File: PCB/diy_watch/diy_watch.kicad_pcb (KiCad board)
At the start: 4 copper layers, 35.9 x 36.9 mm, 48 parts, among them IC1 W25Q16JVUXIQ, J1 USB_B_Micro, SW1 SW_Push, U1 FTE-2CA-V-T/R, U2 DS3231MZ, U3 RP2040, U7 XC6210B332MR, U8 LTC4071EMS8E_PBF, Y1 12MHz_crystal

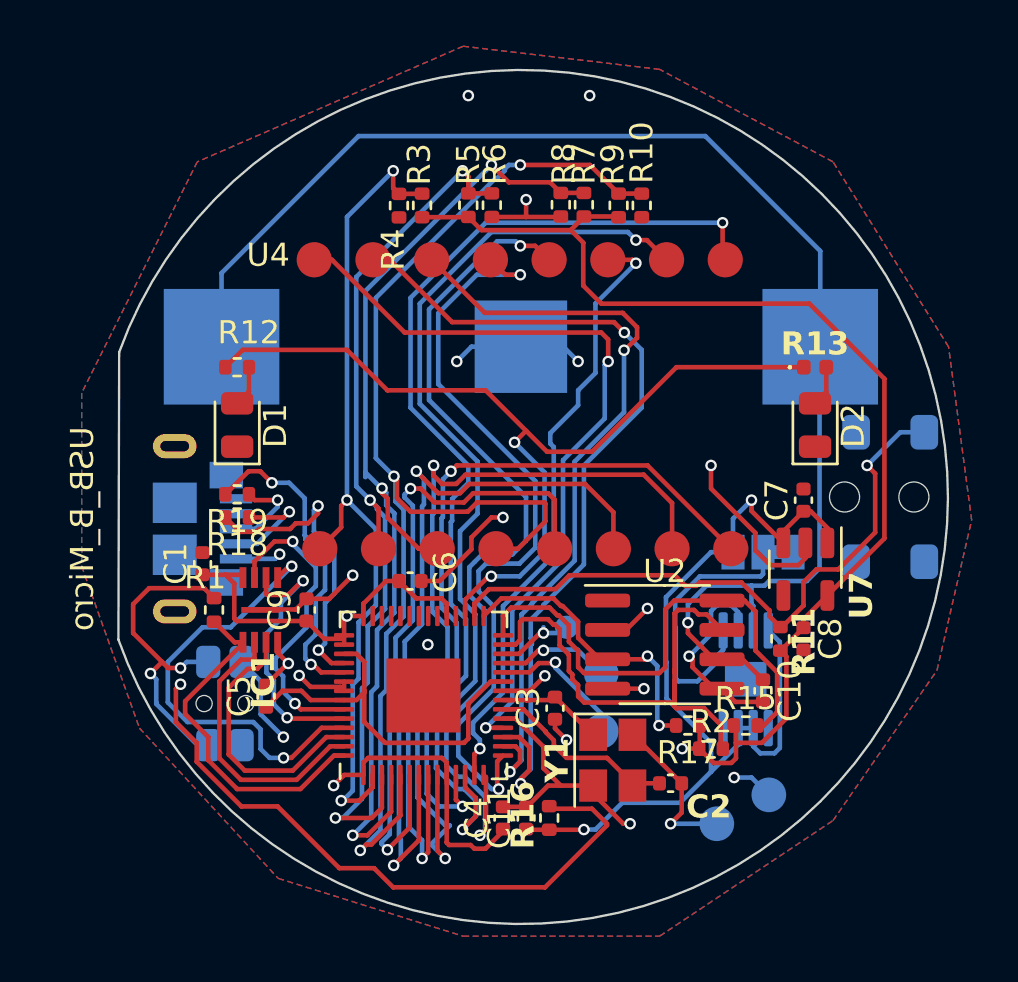
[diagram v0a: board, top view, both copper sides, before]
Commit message: Fixing ERC and DRC errors
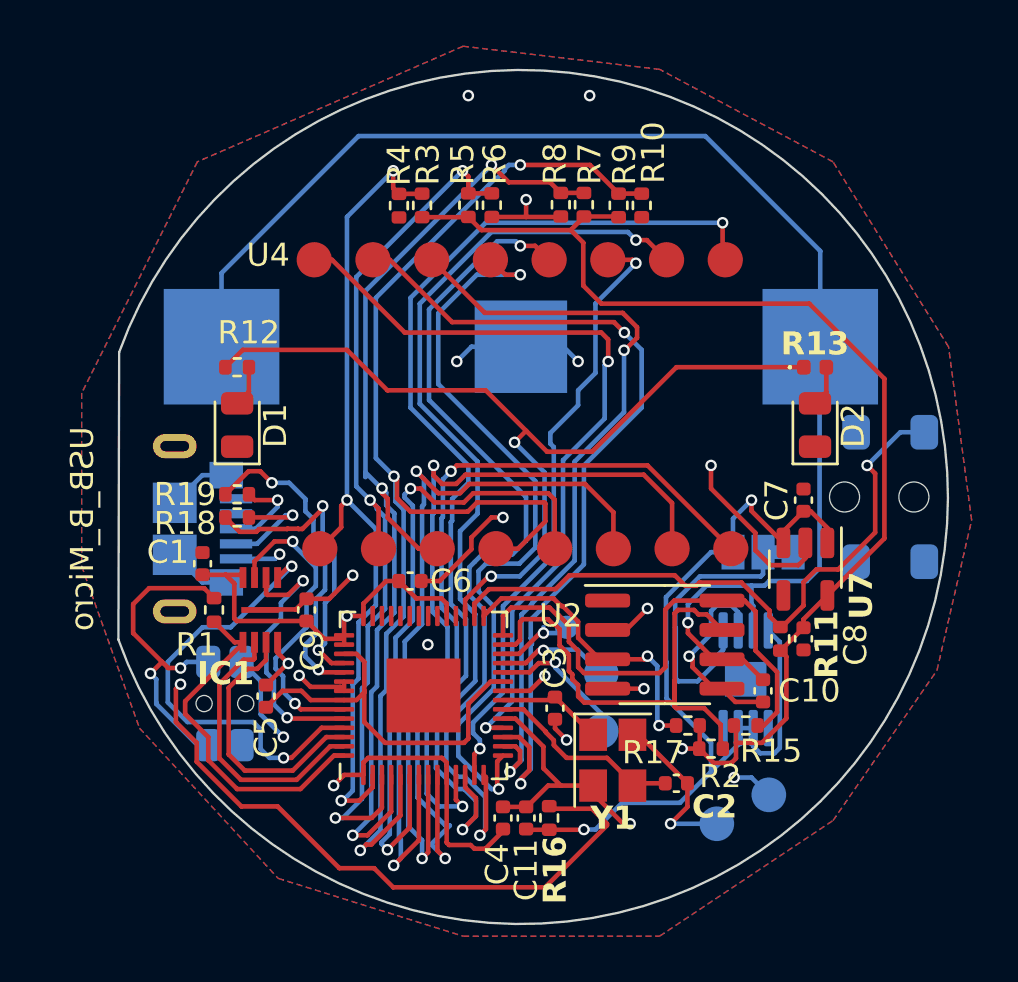
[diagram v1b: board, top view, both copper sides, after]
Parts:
- moved C2 0.25 mm to (156.7, 112.4)
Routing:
- net GND: track 62.5 -> 66.9 mm

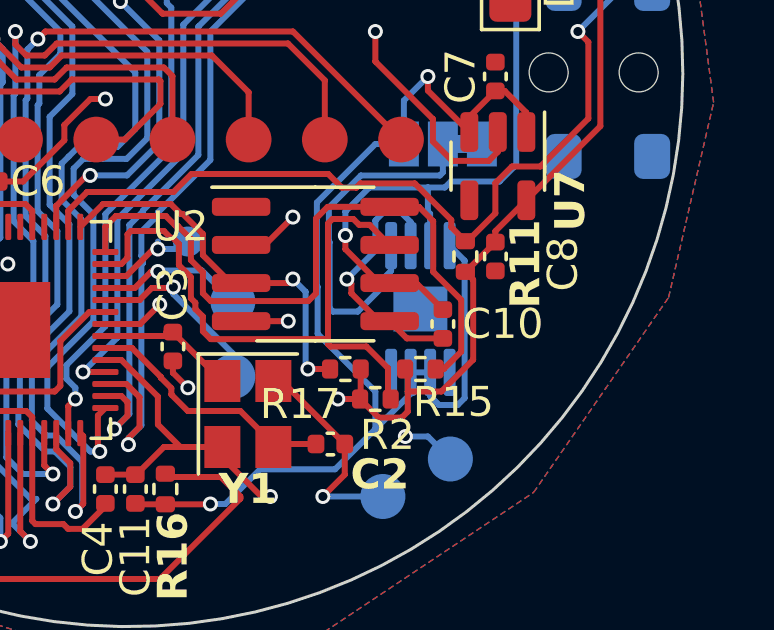
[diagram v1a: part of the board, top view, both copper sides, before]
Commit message: Fixing DRC warnings
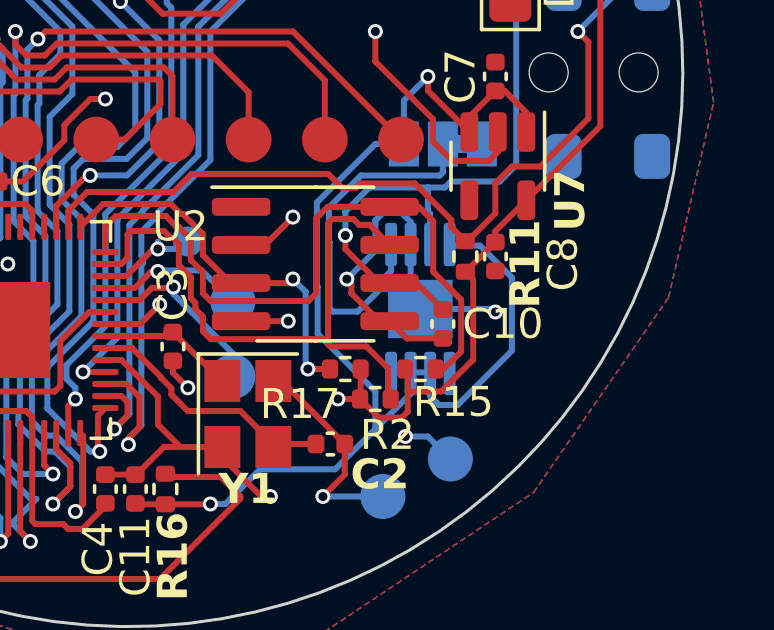
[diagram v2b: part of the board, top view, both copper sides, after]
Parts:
- U8: footprint Package_SO:MSOP-8-1EP_3x3mm_P0.65mm_EP1.5x1.8mm -> Package_SO:MSOP-8-1EP_3x3mm_P0.65mm_EP1.95x2.15mm
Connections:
- net /usb_D+ renamed Net-(J1-D+)
- net /usb_D- renamed Net-(J1-D-)
- U8 pad 9: (no net) -> GND
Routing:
- net GND: track 66.9 -> 71.7 mm, vias 15 -> 16
- net VCC: track 40.3 -> 42.2 mm

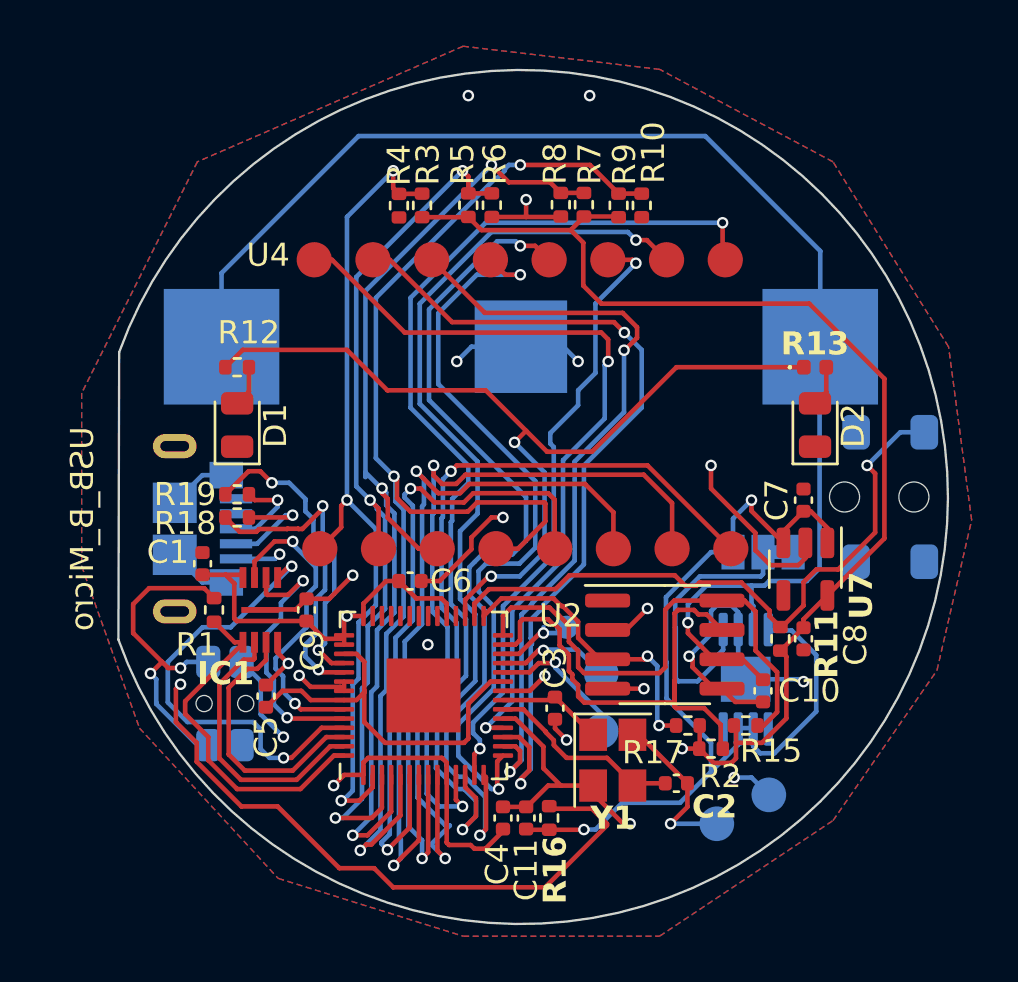
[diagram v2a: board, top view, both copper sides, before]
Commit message: Added mounting piont cutouts to PCB
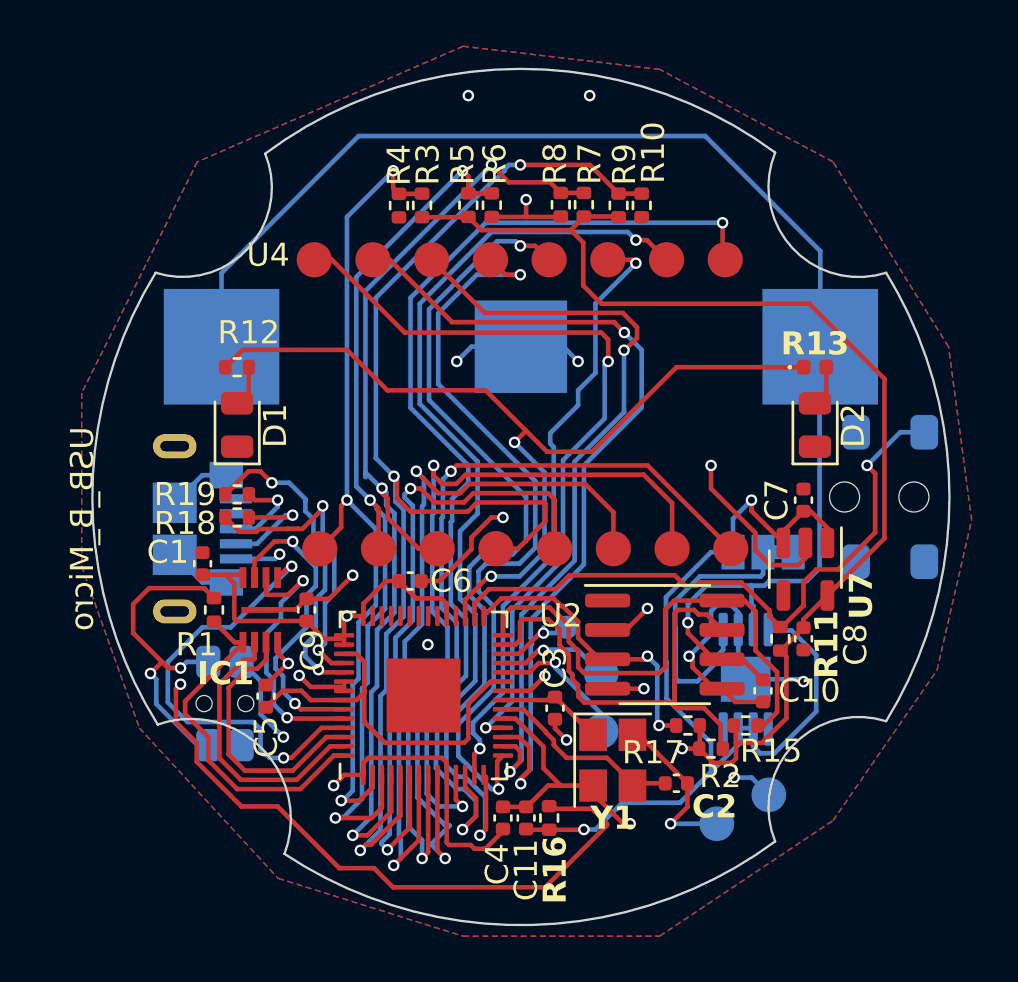
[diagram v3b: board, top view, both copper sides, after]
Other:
- board size 35.9 x 36.9 mm -> 37.1 x 37 mm
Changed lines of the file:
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@@
 		(pad_to_mask_clearance 0.038)
 		(allow_soldermask_bridges_in_footprints no)
-		(grid_origin 149.225 103.886)
+		(grid_origin 150 100)
 		(pcbplotparams
 			(layerselection 0x00010fc_ffffffff)
@@
 	)
 	(gr_arc
-		(start 132.620297 93.737637)
-		(mid 168.473467 100.04798)
-		(end 132.588002 106.172001)
+		(start 161 114.9)
+		(mid 161.743617 110.771032)
+		(end 165.799999 109.7)
 		(stroke
 			(width 0.1)
@@
 		(layer "Edge.Cuts")
 	)
-	(gr_line
-		(start 132.588 106.172)
-		(end 132.620296 93.737637)
+	(gr_arc
+		(start 134.289332 109.844026)
+		(mid 131.460239 100.08474)
+		(end 134.200002 90.300001)
+		(stroke
+			(width 0.1)
+			(type default)
+		)
+		(layer "Edge.Cuts")
+	)
+	(gr_arc
+		(start 134.289332 109.844026)
+		(mid 138.813922 110.895675)
+		(end 139.772981 115.440793)
+		(stroke
+			(width 0.1)
+			(type default)
+		)
+		(layer "Edge.Cuts")
+	)
+	(gr_arc
+		(start 138.935587 85.147769)
+		(mid 149.959903 81.479514)
+		(end 161 85.1)
 		(stroke
 			(width 0.1)
@@
 		(layer "Edge.Cuts")
 	)
+	(gr_arc
+		(start 165.8 90.3)
+		(mid 161.743616 89.228969)
+		(end 161 85.1)
+		(stroke
+			(width 0.1)
+			(type default)
+		)
+		(layer "Edge.Cuts")
+	)
+	(gr_arc
+		(start 161 114.9)
+		(mid 150.471687 118.514522)
+		(end 139.772981 115.440793)
+		(stroke
+			(width 0.1)
+			(type default)
+		)
+		(layer "Edge.Cuts")
+	)
+	(gr_arc
+		(start 165.799999 90.3)
+		(mid 168.539956 100)
+		(end 165.799999 109.7)
+		(stroke
+			(width 0.1)
+			(type default)
+		)
+		(layer "Edge.Cuts")
+	)
+	(gr_arc
+		(start 138.935587 85.147769)
+		(mid 138.20896 89.232335)
+		(end 134.200001 90.3)
+		(stroke
+			(width 0.1)
+			(type default)
+		)
+		(layer "Edge.Cuts")
+	)
+	(gr_circle
+		(center 150 100)
+		(end 165 100)
+		(stroke
+			(width 0.2)
+			(type default)
+		)
+		(fill none)
+		(layer "F.Fab")
+	)
+	(gr_circle
+		(center 150 100)
+		(end 168.5 100)
+		(stroke
+			(width 0.2)
+			(type default)
+		)
+		(fill none)
+		(layer "F.Fab")
+	)
 	(segment

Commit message: Rerouted with new spaces for back mounting
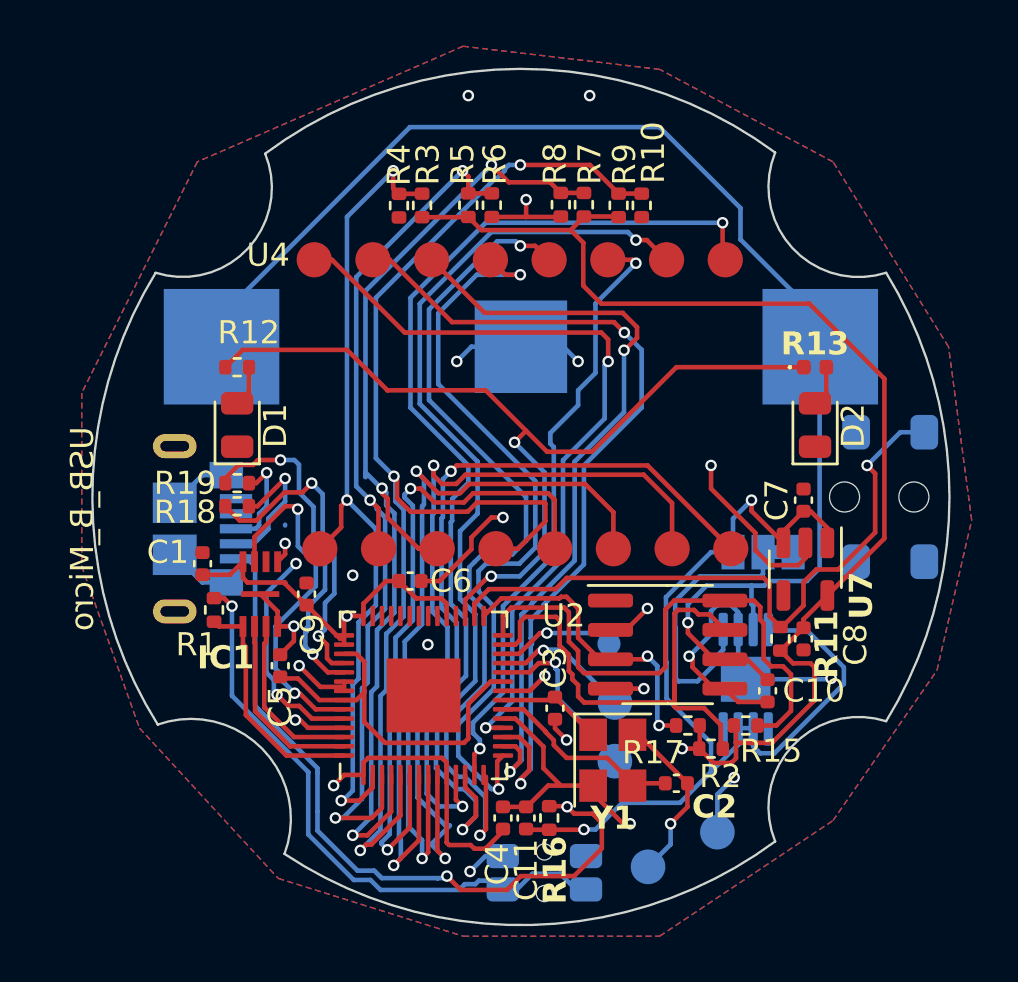
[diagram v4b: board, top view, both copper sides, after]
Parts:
- moved SW1 15.6 mm to (151.0, 116.3), turned to 180 degrees
- moved TP2 3.51 mm to (155.5, 116.0)
- moved TP5 2.75 mm to (158.5, 114.5)
- moved TP4 1.97 mm to (153.8, 106.3)
- moved C5 1.45 mm to (139.6, 107.3)
- moved TP1 1.42 mm to (154.1, 111.4)
- moved TP3 1.39 mm to (154.1, 108.9)
- moved C9 0.69 mm to (140.7, 104.2)
- moved IC1 0.69 mm to (138.7, 104.2)
- moved R18 0.49 mm to (137.7, 100.4)
- moved R19 0.49 mm to (137.7, 99.4)
- moved C10 0.19 mm to (160.7, 108.4)
- moved U2 0.12 mm to (156.3, 106.4)
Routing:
- net Net-(IC1-DI_(IO0)): track 19.3 -> 3.17 mm
- net Net-(R1-Pad1): track 14.3 -> 26.1 mm, vias 2 -> 1
- net +5V: track 37.8 -> 32.1 mm
- net Net-(IC1-~{CS}): track 15.3 -> 10.2 mm
- net Net-(IC1-~{WP_}(IO2)): track 11.6 -> 7.51 mm
- net Net-(IC1-DO_(IO1)): track 12.3 -> 8.16 mm
- net GND: track 71.7 -> 67.8 mm
- net Net-(IC1-CLK): track 12.0 -> 9.72 mm
- net +3.3V: track 127.5 -> 129.5 mm
- net Net-(IC1-(IO3)): track 13.4 -> 15.3 mm
- net /RTC_SCL: track 22.8 -> 24.5 mm
- net Net-(U3-RUN): track 3.48 -> 5.15 mm
- net Net-(U3-SWCLK): track 6.25 -> 7.79 mm
- net +BATT: track 61.0 -> 59.5 mm
- net VCC: track 42.2 -> 43.6 mm
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
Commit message: More DRC corrections
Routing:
- net +5V: vias 2 -> 1

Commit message: DRC Fixes
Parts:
- moved C3 0.16 mm to (151.5, 109.3)
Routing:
- net Net-(IC1-DI_(IO0)): track 3.17 -> 12.6 mm
- net Net-(IC1-CLK): track 9.72 -> 14.4 mm
- net GND: track 67.8 -> 70.7 mm
- net Net-(JP1-C): track 12.4 -> 11.8 mm
- net Net-(IC1-~{WP_}(IO2)): track 7.51 -> 8.19 mm
- net Net-(IC1-DO_(IO1)): track 8.16 -> 8.81 mm
- net Net-(IC1-~{CS}): track 10.2 -> 10.8 mm

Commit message: More DRC fixes
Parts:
- JP1: footprint Jumper:SolderJumper-3_P1.3mm_Bridged12_Pad1.0x1.5mm -> Jumper:SolderJumper-3_P1.3mm_Bridged12_RoundedPad1.0x1.5mm
- moved JP1 0.29 mm to (160.2, 102.3)
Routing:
- net GND: track 70.7 -> 75.2 mm, vias 16 -> 32
- net /COM4: track 55.0 -> 55.5 mm
